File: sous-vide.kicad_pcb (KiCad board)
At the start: 2 copper layers, 95 x 68 mm, 27 parts, among them J2 Conn_01x02, J3 Conn_01x02, J4 Conn_01x03, J5 Conn_01x02, Q1 2N3904, SW1 SW_Push_Dual, SW2 SW_Push_Dual, U1 node_mcu1.0, U2 RAC01, U3 G5LE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

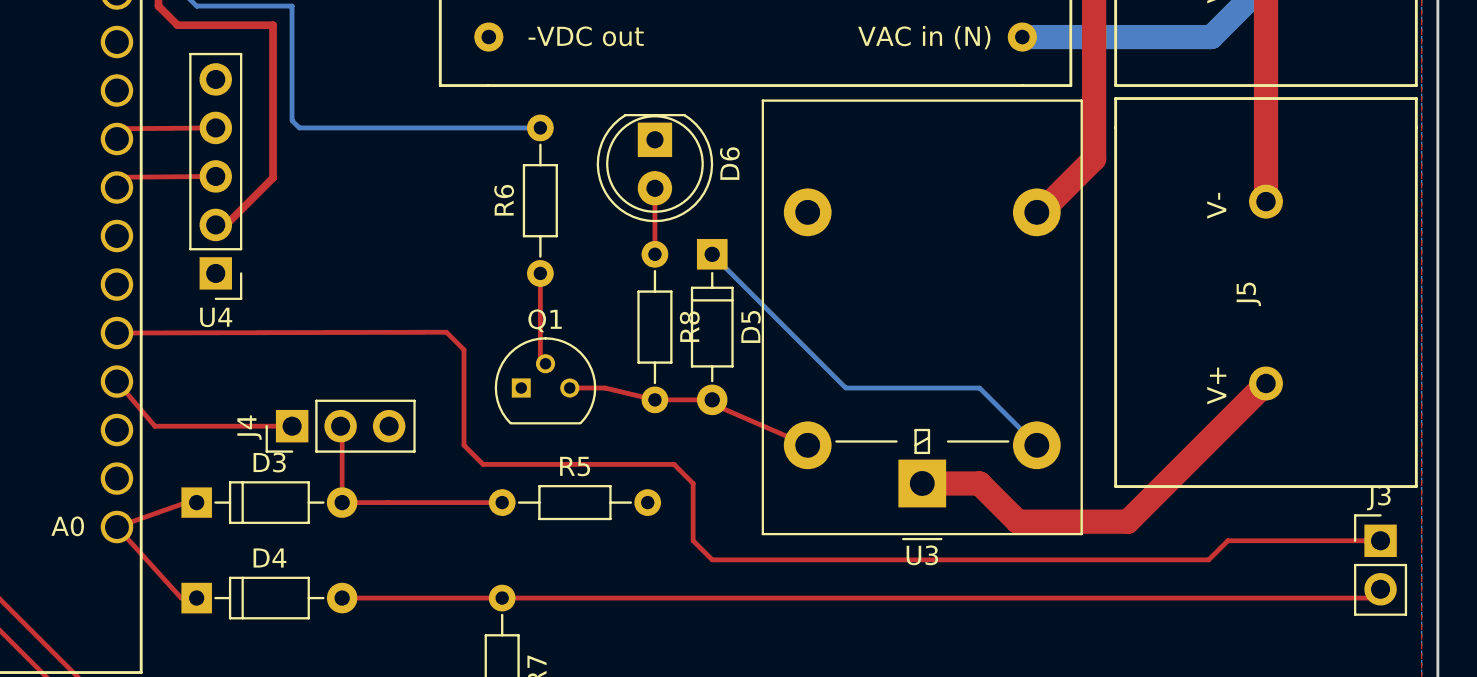
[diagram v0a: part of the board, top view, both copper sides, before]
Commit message: added correct potentiometer footprint
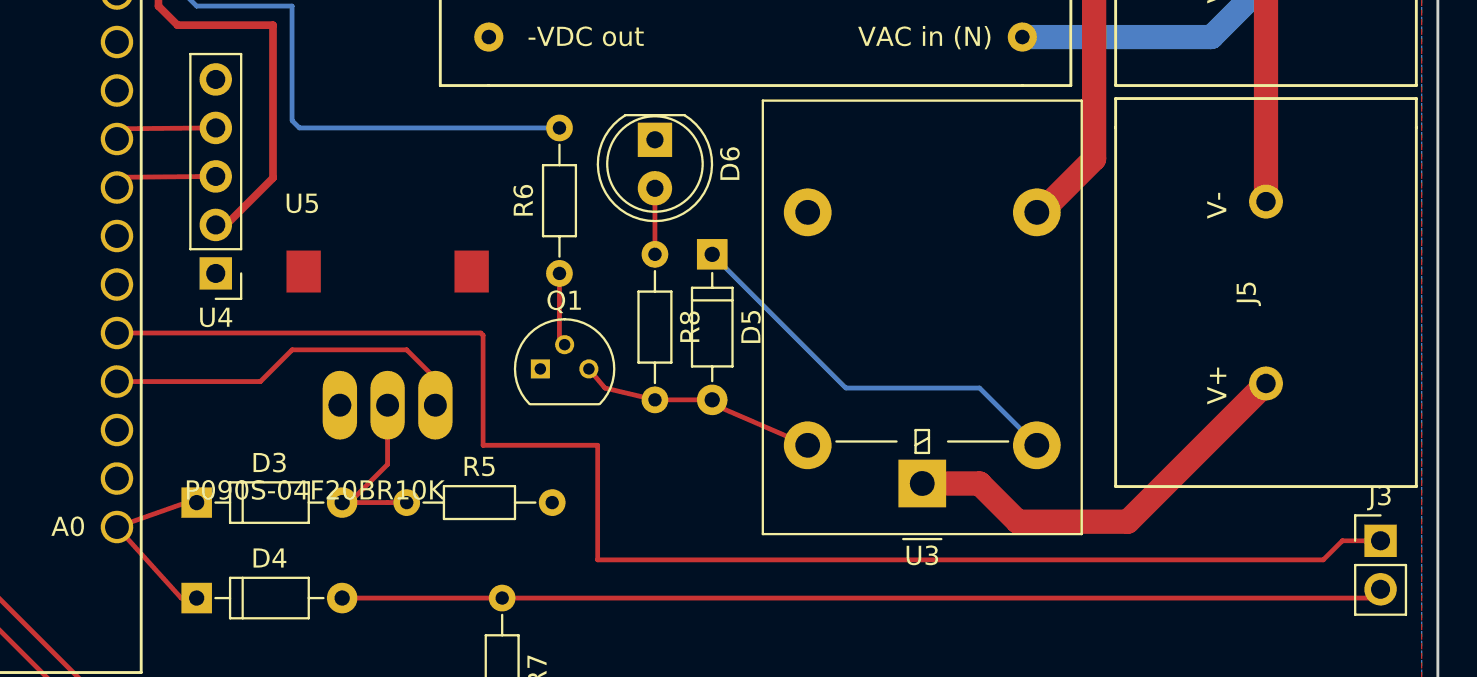
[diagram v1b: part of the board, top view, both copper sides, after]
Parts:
- removed J4: Conn_01x03, Pin_Headers:Pin_Header_Straight_1x03_Pitch2.54mm
- added U5: P090S-04F20BR10K, P090S-04F20BR10K:TRIM_P090S-04F20BR10K, F.Cu at (146.0, 69.0)
- moved R5 5.00 mm to (147.0, 80.0)
- moved Q1 1.41 mm to (154.0, 73.0)
- moved R6 1.00 mm to (155.0, 68.0)
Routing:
- net Net-(U1-Pad4): track 10.4 -> 20.9 mm
- net Net-(D3-Pad2): track 12.4 -> 9.69 mm
- net Net-(J3-Pad1): track 77.1 -> 79.2 mm
- net Net-(R6-Pad2): track 65.7 -> 66.7 mm
- net Net-(Q1-Pad2): track 4.84 -> 3.84 mm
- net Net-(D5-Pad2): track 13.1 -> 12.6 mm

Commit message: redo entire schematic and layout
now complete with danger zone!
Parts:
- removed J5: Conn_01x02, custom:NC6-P108-02
- removed R7: 11k, Resistors_THT:R_Axial_DIN0204_L3.6mm_D1.6mm_P7.62mm_Horizontal
- removed R8: 100, Resistors_THT:R_Axial_DIN0204_L3.6mm_D1.6mm_P7.62mm_Horizontal
- removed REF** (x2): MountingHole_3.2mm_M3, Mounting_Holes:MountingHole_3.2mm_M3
- added J1: Conn_01x02, custom:NC6-P108-02, F.Cu at (115.0, 69.0)
- added MT1: MountingHole_3.2mm_M3, Mounting_Holes:MountingHole_3.2mm_M3, F.Cu at (165.0, 45.0)
- added MT2: MountingHole_3.2mm_M3, Mounting_Holes:MountingHole_3.2mm_M3, F.Cu at (190.0, 95.0)
- D1, D2: value LED -> D; footprint LEDs:LED_D5.0mm -> Diodes_THT:D_DO-35_SOD27_P7.62mm_Horizontal
- D3, D5: value D -> LED; footprint Diodes_THT:D_DO-35_SOD27_P7.62mm_Horizontal -> LEDs:LED_D5.0mm
- R1: value 11k -> 110
- R3: value 100 -> 1k
- R4: value 100 -> 41
- R5: value 11k -> 41
- R6: value 1k -> 11k
- U1: value node_mcu1.0 -> G5LE; footprint custom:NodeMCU_1_0 -> Relays_THT:Relay_SPDT_OMRON-G5LE-1
- U3: value G5LE -> node_mcu1.0; footprint Relays_THT:Relay_SPDT_OMRON-G5LE-1 -> custom:NodeMCU_1_0
- U4: value LCD_Backpack -> P090S; footprint Pin_Headers:Pin_Header_Straight_1x05_Pitch2.54mm -> P090S-04F20BR10K:TRIM_P090S-04F20BR10K
- U5: value P090S-04F20BR10K -> LCD_Backpack; footprint P090S-04F20BR10K:TRIM_P090S-04F20BR10K -> Pin_Headers:Pin_Header_Straight_1x05_Pitch2.54mm
- moved J2 77.0 mm to (115.0, 48.0), turned to 90 degrees
- moved D2 65.5 mm to (167.0, 65.0), turned to 270 degrees
- moved D6 51.7 mm to (125.0, 99.0), turned to 0 degrees
- moved D1 49.0 mm to (172.0, 102.0), turned to 180 degrees
- moved R4 45.0 mm to (154.0, 93.0)
- moved R3 43.8 mm to (159.0, 73.0), turned to 90 degrees
- moved D4 39.5 mm to (175.0, 91.0)
- moved U4 35.8 mm to (168.0, 86.0), turned to 0 degrees
- moved R1 35.8 mm to (163.0, 73.0), turned to 90 degrees
- moved R2 34.4 mm to (164.0, 97.0)
- moved R6 33.6 mm to (175.0, 95.0), turned to 0 degrees
- moved D5 32.6 mm to (157.0, 99.0), turned to 0 degrees
- moved R5 27.3 mm to (123.0, 93.0)
- moved U5 25.2 mm to (171.0, 66.0), turned to 180 degrees
- moved U1 23.8 mm to (144.0, 69.0), turned to 270 degrees
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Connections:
- D1 pad 1: GND -> /A0
- D2 pad 1: GND -> +5V
- D3 pad 1: Net-(D3-Pad1) -> GND
- D4 pad 1: Net-(D3-Pad1) -> /A0
- D5 pad 1: Net-(D5-Pad1) -> GND
- J2 pad 2: Net-(J2-Pad2) -> Net-(J1-Pad2)
- J3 pad 1: Net-(J3-Pad1) -> /THERMISTOR
- Q1 pad 3: Net-(D5-Pad2) -> Net-(D2-Pad2)
- R1 pad 1: Net-(R1-Pad1) -> Net-(D2-Pad2)
- R1 pad 2: GND -> Net-(D3-Pad2)
- R2 pad 1: Net-(R2-Pad1) -> Net-(D1-Pad2)
- R3 pad 1: Net-(R3-Pad1) -> Net-(Q1-Pad2)
- R3 pad 2: Net-(D1-Pad2) -> Net-(R3-Pad2)
- R4 pad 1: Net-(R4-Pad1) -> /RED_LED
- R4 pad 2: Net-(D2-Pad2) -> Net-(D5-Pad2)
- R5 pad 1: Net-(D3-Pad2) -> /BLUE_LED
- R5 pad 2: GND -> Net-(D6-Pad2)
- R6 pad 1: Net-(Q1-Pad2) -> GND
- R6 pad 2: Net-(R6-Pad2) -> Net-(D4-Pad2)
- SW1 pad 1: +3V3 -> Net-(SW1-Pad1)
- SW1 pad 2: Net-(R1-Pad1) -> Net-(SW1-Pad2)
- SW1 pad 3: +3V3 -> /SW1
- SW1 pad 4: Net-(SW1-Pad4) -> GND
- SW2 pad 1: +3V3 -> /SW2
- SW2 pad 2: Net-(R2-Pad1) -> GND
- SW2 pad 3: +3V3 -> Net-(SW2-Pad3)
- U1 pad 1: Net-(D3-Pad1) -> Net-(J1-Pad1)
- U1 pad 2: Net-(U1-Pad2) -> +5V
- U1 pad 3: Net-(U1-Pad3) -> Net-(J2-Pad1)
- U1 pad 5: Net-(J3-Pad1) -> Net-(D2-Pad2)
- U2 pad 2: Net-(J2-Pad2) -> Net-(J1-Pad2)
- U3 pad 1: Net-(J5-Pad1) -> /A0
- U3 pad 2: Net-(D5-Pad1) -> (no net)
- U3 pad 3: Net-(J2-Pad2) -> (no net)
- U3 pad 4: Net-(U3-Pad4) -> (no net)
- U3 pad 5: Net-(D5-Pad2) -> (no net)
- U4 pad 2: +5V -> Net-(D1-Pad2)
- U4 pad 3: Net-(U1-Pad8) -> /UESR_POT
- U5 pad 2: Net-(D3-Pad2) -> +5V
- U5 pad 3: Net-(U1-Pad4) -> /CLK
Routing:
- net Net-(J3-Pad1): track 79.2 -> 0.00 mm
- net Net-(R6-Pad2): track 66.7 -> 0.00 mm
- net /BLUE_LED: track 0.00 -> 61.9 mm
- net +5V: track 47.8 -> 106.7 mm
- net Net-(SW1-Pad4): track 56.9 -> 0.00 mm
- net /SW2: track 0.00 -> 48.5 mm
- net /SW1: track 0.00 -> 44.3 mm
- net /A0: track 0.00 -> 42.2 mm
- net Net-(J2-Pad2): track 41.3 -> 0.00 mm
- net Net-(D4-Pad2): track 54.6 -> 21.3 mm
- net Net-(J1-Pad1): track 0.00 -> 31.0 mm
- net Net-(SW2-Pad4): track 29.9 -> 0.00 mm
- net /THERMISTOR: track 0.00 -> 29.6 mm
- net /RED_LED: track 0.00 -> 28.2 mm
- net Net-(R3-Pad2): track 0.00 -> 27.2 mm
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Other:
- net class VAC: clearance 1 -> 2.5; trace_width 1.27 -> 2.5
- board text added: "DANGER ZONE"
- board text removed: "Sous-Vide V0.1"

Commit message: new PCB cad
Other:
- board text added: "Des Trucs Sous Vide!"
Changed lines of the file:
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@@
     (area 105.924999 36.924999 201.075001 105.075001)
     (thickness 1.6)
-    (drawings 8)
+    (drawings 9)
     (tracks 121)
     (zones 0)
@@
     (pad 1 np_thru_hole circle (at 0 0) (size 3.2 3.2) (drill 3.2) (layers *.Cu *.Mask))
   )
+  (gr_text "Des Trucs Sous Vide!" (at 129 83) (layer B.SilkS)
+    (effects (font (size 3 2.5) (thickness 0.3) italic) (justify mirror))
+  )
   (gr_text "DANGER ZONE" (at 122 82) (layer F.SilkS)

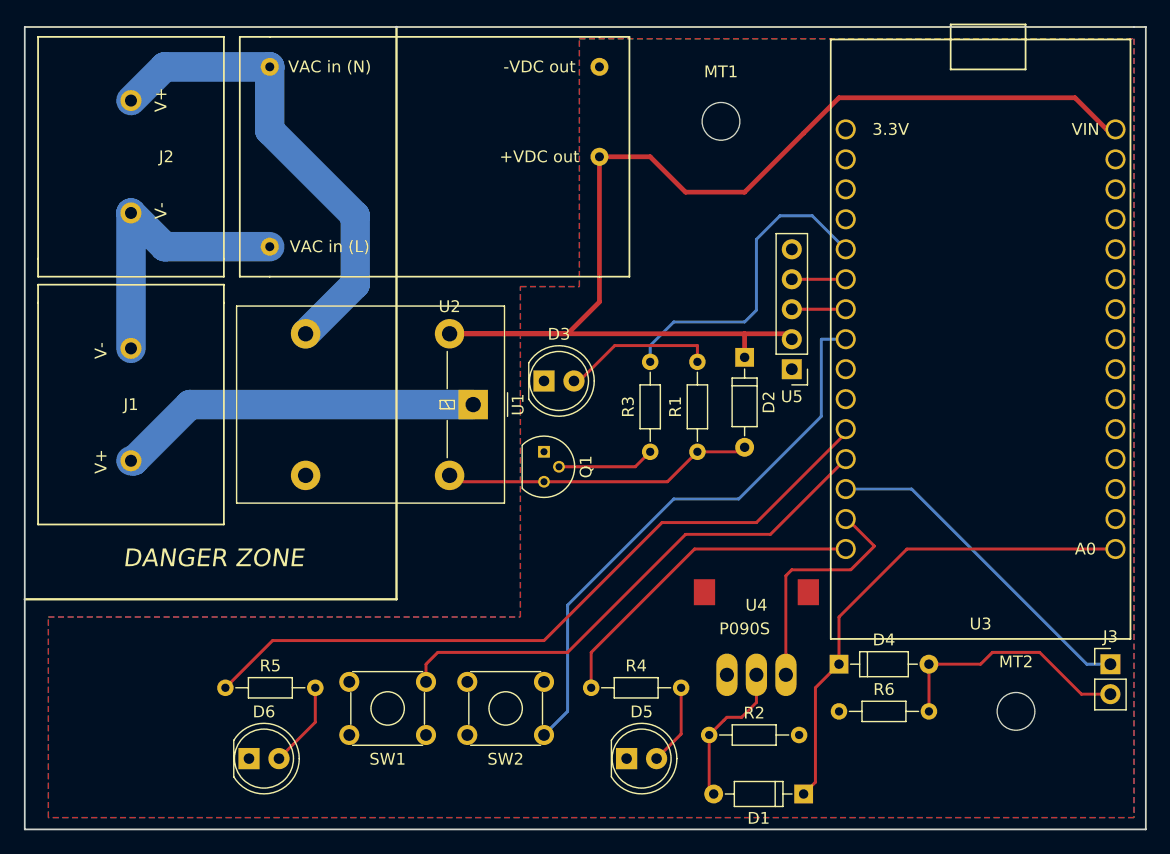
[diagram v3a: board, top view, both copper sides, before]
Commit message: fix DRC issues
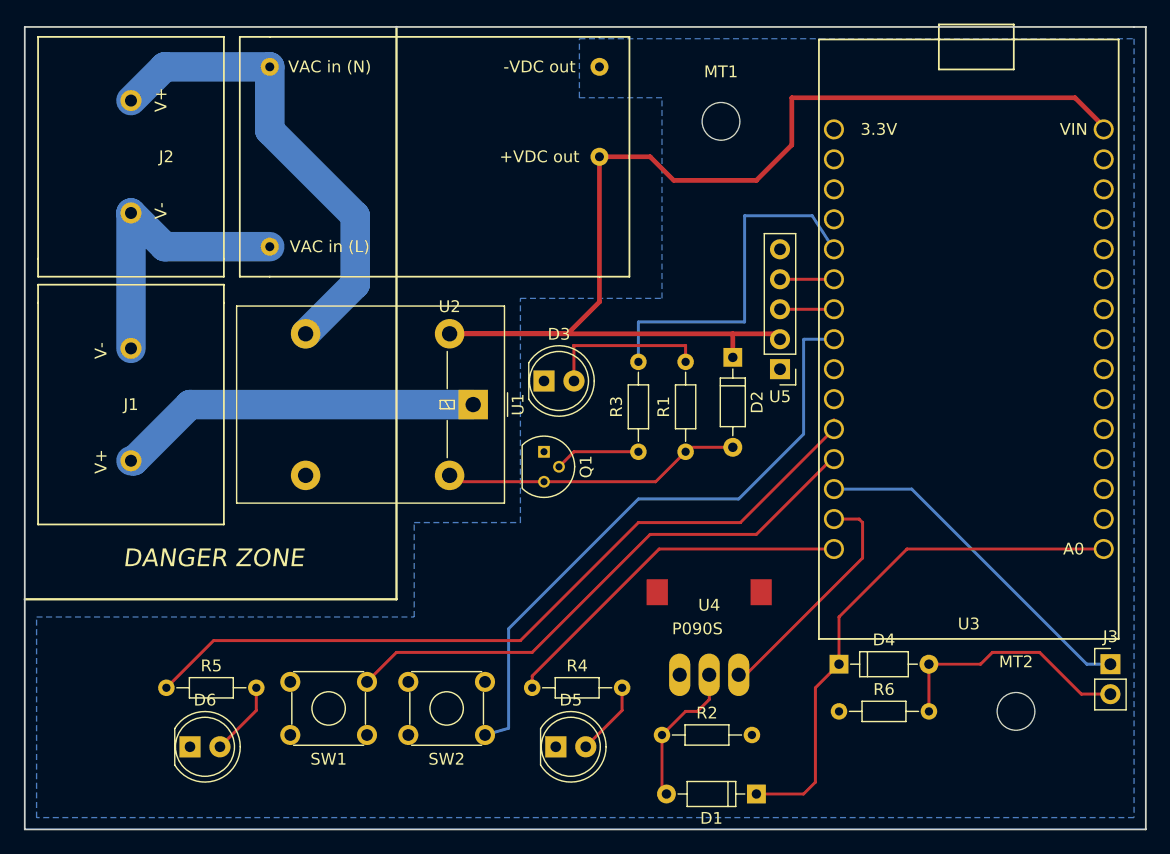
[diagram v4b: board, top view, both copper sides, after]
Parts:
- moved D5 6.08 mm to (151.0, 98.0)
- moved D6 5.10 mm to (120.0, 98.0)
- moved R4 5.00 mm to (149.0, 93.0)
- moved R5 5.00 mm to (118.0, 93.0)
- moved SW1 5.00 mm to (135.0, 97.0)
- moved SW2 5.00 mm to (145.0, 97.0)
- moved D1 4.00 mm to (168.0, 102.0)
- moved R2 4.00 mm to (160.0, 97.0)
- moved U4 4.00 mm to (164.0, 86.0)
- moved D2 1.00 mm to (166.0, 65.0)
- moved R1 1.00 mm to (162.0, 73.0)
- moved R3 1.00 mm to (158.0, 73.0)
- moved U3 1.00 mm to (186.0, 66.0)
- moved U5 1.00 mm to (170.0, 66.0)
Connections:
- U3 pad 11: +3V3 -> Net-(U3-Pad11)
- U3 pad 21: +3V3 -> Net-(U3-Pad21)
- U3 pad 30: +3V3 -> Net-(U3-Pad30)
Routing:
- net /BLUE_LED: track 61.9 -> 66.5 mm
- net /SW2: track 48.5 -> 52.9 mm
- net Net-(R3-Pad2): track 27.2 -> 30.5 mm
- net /SW1: track 44.3 -> 47.4 mm
- net /RED_LED: track 28.2 -> 31.1 mm
- net /A0: track 42.2 -> 45.1 mm
- net (no net): track 2.56 -> 0.00 mm
- net Net-(D3-Pad2): track 13.1 -> 14.4 mm
- net /UESR_POT: track 21.7 -> 20.7 mm
- net Net-(D6-Pad2): track 7.28 -> 6.28 mm
- net /THERMISTOR: track 29.6 -> 30.6 mm
- net Net-(D2-Pad2): track 27.5 -> 26.5 mm
- net Net-(Q1-Pad2): track 8.64 -> 7.64 mm
- net Net-(D1-Pad2): track 12.2 -> 13.0 mm
- net Net-(D5-Pad2): track 6.86 -> 6.28 mm
- removed copper zone on F.Cu, net +3V3
